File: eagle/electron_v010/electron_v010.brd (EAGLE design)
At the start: 20.3 x 50.8 mm, 92 parts, among them J1 SIM-NANO-4FF, J2 IPEX-20279-001E, U1 U-BLOX-SARA-U260, U2 SN74AVC4T245, U3 STM32F205RG, U4 MAX1704X, U5 SN74LVC1G07, U6 SN74LVC1G07, U8 SN74AVC4T245, X1 USB-MICROB, Y1 32Khz, Y2 26Mhz

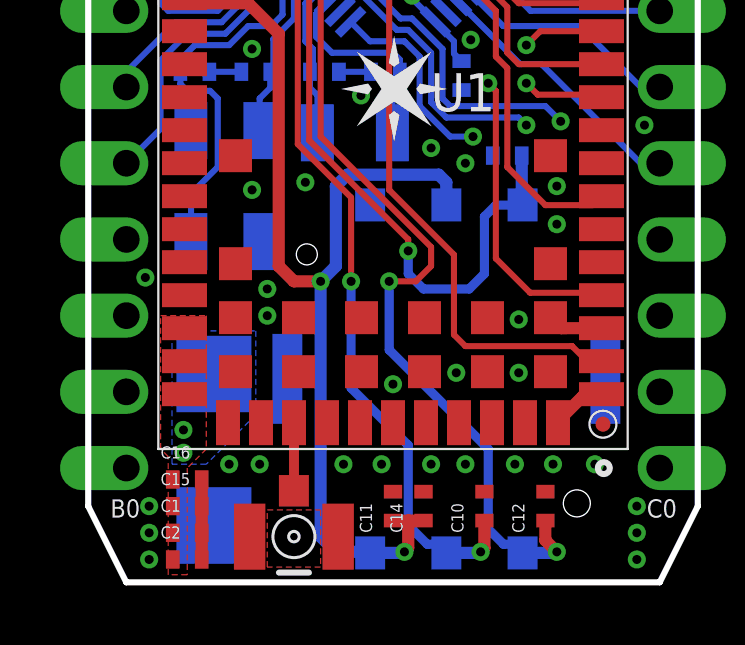
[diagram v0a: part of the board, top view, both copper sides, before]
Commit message: #13 Added more GND Vias around ANT connector and updated trace routes
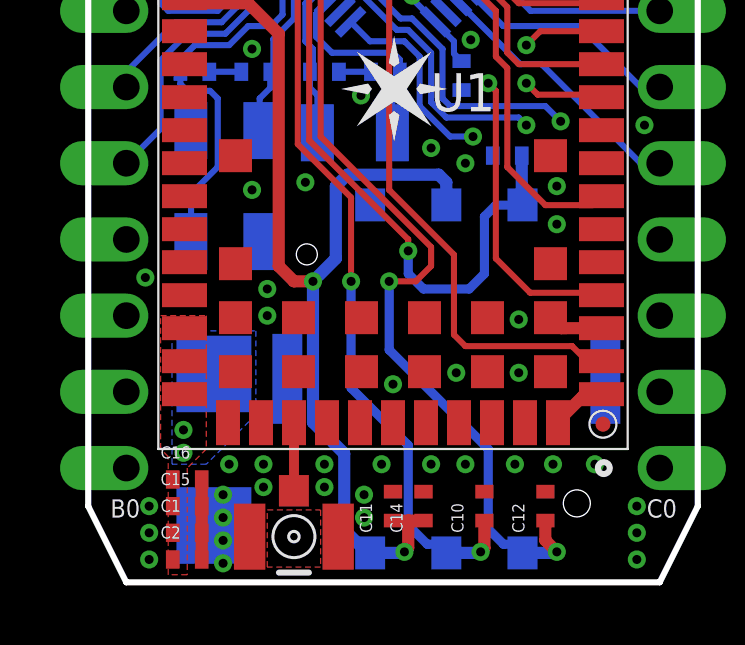
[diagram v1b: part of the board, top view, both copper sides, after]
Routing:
- net SIM_VCC: track 34.7 -> 34.1 mm
- net GND: vias 54 -> 62
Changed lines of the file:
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@@
 <layer number="21" name="tPlace" color="16" fill="1" visible="yes" active="yes"/>
 <layer number="22" name="bPlace" color="14" fill="1" visible="no" active="yes"/>
-<layer number="23" name="tOrigins" color="15" fill="1" visible="yes" active="yes"/>
-<layer number="24" name="bOrigins" color="15" fill="1" visible="yes" active="yes"/>
+<layer number="23" name="tOrigins" color="15" fill="1" visible="no" active="yes"/>
+<layer number="24" name="bOrigins" color="15" fill="1" visible="no" active="yes"/>
 <layer number="25" name="tNames" color="7" fill="1" visible="no" active="yes"/>
 <layer number="26" name="bNames" color="7" fill="1" visible="no" active="yes"/>
@@
 <via x="4.699" y="3.937" extent="1-16" drill="0.3"/>
 <via x="14.224" y="3.937" extent="1-16" drill="0.3"/>
-<via x="8.509" y="3.937" extent="1-16" drill="0.3"/>
+<via x="7.874" y="3.937" extent="1-16" drill="0.3"/>
 <via x="9.779" y="3.937" extent="1-16" drill="0.3"/>
-<via x="5.715" y="3.937" extent="1-16" drill="0.3"/>
+<via x="5.842" y="3.937" extent="1-16" drill="0.3"/>
 <via x="12.573" y="3.937" extent="1-16" drill="0.3"/>
 <via x="11.43" y="3.937" extent="1-16" drill="0.3"/>
@@
 <via x="18.0848" y="43.4594" extent="1-16" drill="0.3"/>
 <contactref element="JP2" pad="15"/>
+<via x="9.1948" y="2.159" extent="1-16" drill="0.3"/>
+<via x="5.842" y="3.175" extent="1-16" drill="0.3"/>
+<via x="7.874" y="3.175" extent="1-16" drill="0.3"/>
+<via x="9.1948" y="2.921" extent="1-16" drill="0.3"/>
+<via x="4.4958" y="2.159" extent="1-16" drill="0.3"/>
+<via x="4.4958" y="2.921" extent="1-16" drill="0.3"/>
+<via x="4.4958" y="1.397" extent="1-16" drill="0.3"/>
+<via x="4.4958" y="0.635" extent="1-16" drill="0.3"/>
 </signal>
 <signal name="N$8">
@@
 <contactref element="C14" pad="1"/>
 <wire x1="10.16" y1="2.0574" x2="10.668" y2="2.0574" width="0.4064" layer="1"/>
-<via x="7.747" y="10.033" extent="1-16" drill="0.3"/>
+<via x="7.493" y="10.033" extent="1-16" drill="0.3"/>
 <wire x1="10.668" y1="2.0574" x2="11.176" y2="2.0574" width="0.4064" layer="1"/>
 <wire x1="3.21" y1="19.472" x2="3.378" y2="19.304" width="0.4064" layer="1"/>
@@
 <wire x1="11.684" y1="13.589" x2="8.636" y2="13.589" width="0.4064" layer="16"/>
 <wire x1="8.636" y1="13.589" x2="8.255" y2="13.208" width="0.4064" layer="16"/>
-<wire x1="8.255" y1="13.208" x2="8.255" y2="10.541" width="0.4064" layer="16"/>
+<wire x1="8.255" y1="13.208" x2="8.255" y2="10.795" width="0.4064" layer="16"/>
 <wire x1="9.3638" y1="1.016" x2="9.398" y2="0.9818" width="0.4064" layer="16"/>
 <via x="10.541" y="1.016" extent="1-16" drill="0.3"/>
@@
 <wire x1="10.541" y1="1.016" x2="10.668" y2="1.143" width="0.4064" layer="1"/>
 <wire x1="10.668" y1="1.143" x2="10.668" y2="2.0574" width="0.4064" layer="1"/>
-<wire x1="8.255" y1="10.541" x2="7.747" y2="10.033" width="0.4064" layer="16"/>
-<wire x1="6.858" y1="10.033" x2="7.747" y2="10.033" width="0.4064" layer="1"/>
-<wire x1="7.747" y1="1.524" x2="7.747" y2="10.033" width="0.4064" layer="16"/>
 <wire x1="5.334" y1="19.304" x2="6.35" y2="18.288" width="0.4064" layer="1"/>
-<wire x1="9.3638" y1="1.016" x2="8.255" y2="1.016" width="0.4064" layer="16"/>
-<wire x1="8.255" y1="1.016" x2="7.747" y2="1.524" width="0.4064" layer="16"/>
+<wire x1="9.3638" y1="1.016" x2="9.271" y2="1.016" width="0.4064" layer="16"/>
+<wire x1="9.271" y1="1.016" x2="8.5344" y2="1.7526" width="0.4064" layer="16"/>
+<wire x1="8.5344" y1="1.7526" x2="8.5344" y2="4.2926" width="0.4064" layer="16"/>
+<wire x1="6.858" y1="10.033" x2="7.493" y2="10.033" width="0.4064" layer="1"/>
+<wire x1="8.255" y1="10.795" x2="7.493" y2="10.033" width="0.4064" layer="16"/>
+<wire x1="7.493" y1="5.334" x2="7.493" y2="10.033" width="0.4064" layer="16"/>
+<wire x1="7.493" y1="5.334" x2="8.5344" y2="4.2926" width="0.4064" layer="16"/>
 </signal>
 <signal name="SIM_RST">

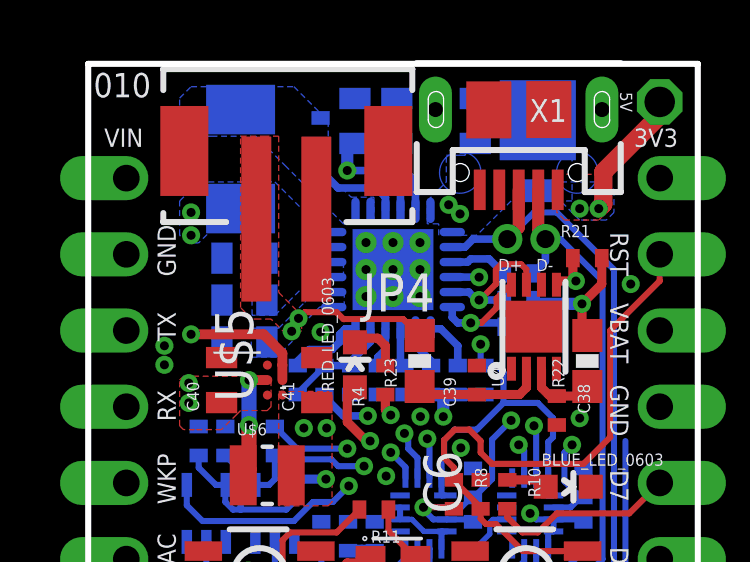
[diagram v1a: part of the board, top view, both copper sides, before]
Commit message: #11 Additional Vias added for battery trace connections
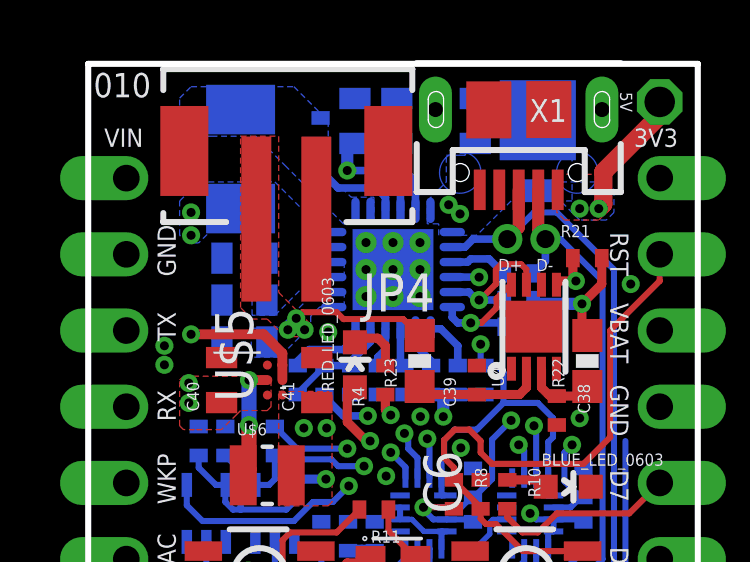
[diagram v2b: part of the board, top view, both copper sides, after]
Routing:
- net BAT: track 4.44 -> 4.52 mm, vias 2 -> 3
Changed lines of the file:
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@@
 </class>
 <class number="3" name="BAT" width="0" drill="0">
-<clearance class="3" value="0.254"/>
+<clearance class="3" value="0.2032"/>
 </class>
 </classes>
@@
 <contactref element="C39" pad="2"/>
 <via x="2.54" y="40.767" extent="1-16" drill="0.3"/>
-<via x="7.747" y="41.8592" extent="1-16" drill="0.3"/>
+<via x="8.001" y="41.8592" extent="1-16" drill="0.3"/>
 <via x="11.0744" y="39.0398" extent="1-16" drill="0.3"/>
 <wire x1="14.351" y1="32.893" x2="13.97" y2="32.893" width="0.2032" layer="16"/>
@@
 <vertex x="7.493" y="45.593"/>
 <vertex x="7.493" y="44.196"/>
-<vertex x="8.509" y="44.196"/>
-<vertex x="8.509" y="43.688"/>
+<vertex x="8.5344" y="44.196"/>
+<vertex x="8.5344" y="43.688"/>
 <vertex x="7.493" y="43.688"/>
 <vertex x="6.223" y="42.418"/>
@@
 <contactref element="JP4" pad="VCC"/>
 <contactref element="R23" pad="2"/>
-<via x="7.0104" y="42.3164" extent="1-16" drill="0.3"/>
+<via x="6.9342" y="42.3164" extent="1-16" drill="0.3"/>
 <wire x1="8.509" y1="42.291" x2="10.502" y2="42.291" width="0.2032" layer="1"/>
 <wire x1="10.502" y1="42.291" x2="11.049" y2="41.744" width="0.2032" layer="1"/>
-<via x="6.7818" y="41.8846" extent="1-16" drill="0.3"/>
+<via x="6.6548" y="41.9354" extent="1-16" drill="0.3"/>
 <wire x1="8.509" y1="42.291" x2="8.2804" y2="42.5196" width="0.2032" layer="1"/>
-<wire x1="8.2804" y1="42.5196" x2="7.2136" y2="42.5196" width="0.2032" layer="1"/>
-<wire x1="7.2136" y1="42.5196" x2="7.0104" y2="42.3164" width="0.2032" layer="1"/>
 <polygon width="0.1524" layer="16" thermals="no" rank="3">
 <vertex x="8.5344" y="43.2054"/>
 <vertex x="8.5344" y="42.6974"/>
-<vertex x="8.4836" y="42.6974"/>
 <vertex x="7.7216" y="42.6974"/>
-<vertex x="7.0358" y="42.0116"/>
-<vertex x="7.0358" y="41.783"/>
-<vertex x="6.2738" y="41.021"/>
+<vertex x="7.4168" y="42.3926"/>
+<vertex x="7.4168" y="41.783"/>
+<vertex x="7.3152" y="41.6814"/>
+<vertex x="7.0358" y="41.6814"/>
+<vertex x="6.3754" y="41.021"/>
 <vertex x="5.4356" y="41.021"/>
-<vertex x="5.4356" y="41.9354"/>
 <vertex x="5.4356" y="41.9862"/>
-<vertex x="5.842" y="41.9862"/>
 <vertex x="6.35" y="41.9862"/>
-<vertex x="7.2136" y="42.8498"/>
 <vertex x="7.5692" y="43.2054"/>
 </polygon>
+<via x="7.2136" y="41.9354" extent="1-16" drill="0.3"/>
+<wire x1="7.1374" y1="42.5196" x2="6.9342" y2="42.3164" width="0.2032" layer="1"/>
 <polygon width="0.1524" layer="1" thermals="no" rank="3">
-<vertex x="6.604" y="41.783"/>
-<vertex x="6.096" y="42.291"/>
-<vertex x="5.715" y="42.291"/>
+<vertex x="5.08" y="48.387"/>
+<vertex x="6.35" y="48.387"/>
+<vertex x="6.35" y="43.18"/>
+<vertex x="7.4168" y="42.1132"/>
+<vertex x="7.4168" y="42.0116"/>
+<vertex x="7.4168" y="41.783"/>
+<vertex x="7.3406" y="41.7068"/>
+<vertex x="6.5532" y="41.7068"/>
+<vertex x="5.969" y="42.291"/>
 <vertex x="5.461" y="42.291"/>
 <vertex x="5.08" y="42.672"/>
-<vertex x="5.08" y="48.387"/>
-<vertex x="5.842" y="48.387"/>
-<vertex x="6.35" y="48.387"/>
-<vertex x="6.35" y="43.18"/>
-<vertex x="6.985" y="42.545"/>
-<vertex x="7.112" y="42.418"/>
-<vertex x="7.112" y="42.164"/>
-<vertex x="7.112" y="41.91"/>
-<vertex x="6.985" y="41.783"/>
 </polygon>
+<wire x1="8.2804" y1="42.5196" x2="7.1374" y2="42.5196" width="0.2032" layer="1"/>
 </signal>
 <signal name="VBUS">
@@
 <contactref element="U$1" pad="12"/>
 <contactref element="R20" pad="2"/>
-<wire x1="8.91" y1="41.967" x2="8.566" y2="41.967" width="0.254" layer="16"/>
-<wire x1="8.566" y1="41.967" x2="8.382" y2="41.783" width="0.254" layer="16"/>
-<wire x1="8.382" y1="41.783" x2="8.382" y2="41.529" width="0.254" layer="16"/>
-<wire x1="8.382" y1="41.529" x2="8.128" y2="41.275" width="0.254" layer="16"/>
-<wire x1="8.128" y1="41.275" x2="7.366" y2="41.275" width="0.254" layer="16"/>
+<wire x1="8.509" y1="41.275" x2="7.366" y2="41.275" width="0.254" layer="16"/>
 <wire x1="7.366" y1="41.275" x2="6.985" y2="40.894" width="0.254" layer="16"/>
 <wire x1="6.985" y1="40.894" x2="6.985" y2="40.7416" width="0.254" layer="16"/>
+<wire x1="8.509" y1="41.275" x2="8.91" y2="41.676" width="0.254" layer="16"/>
+<wire x1="8.91" y1="41.676" x2="8.91" y2="41.967" width="0.254" layer="16"/>
 </signal>
 <signal name="N$7">

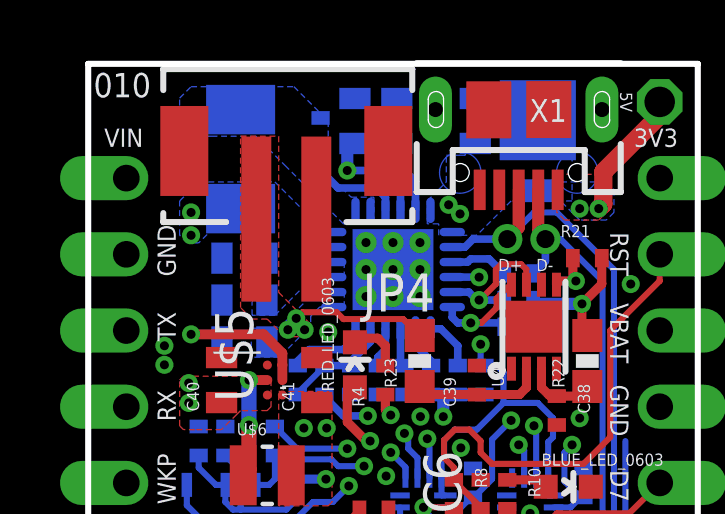
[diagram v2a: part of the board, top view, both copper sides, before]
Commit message: #12 Updated to bigger pads PMIC inductor footprint and power polygons
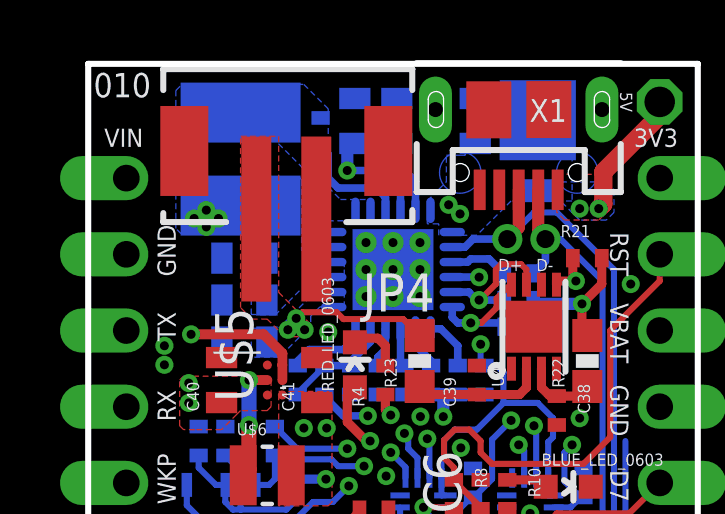
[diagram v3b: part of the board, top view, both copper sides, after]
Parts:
- U$4: device electron:4020TYPE -> Particle:INDUCTOR-4020
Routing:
- net +3V8: track 57.4 -> 56.7 mm, vias 8 -> 10
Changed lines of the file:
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@@
 <element name="JP4" library="SparkFun-Connectors" package="JST-2-SMD-VERT" value="" x="6.604" y="47.625" locked="yes"/>
 <element name="U$3" library="Spark" package="DIODE-DO-220AA(SMP)" value="DIODE" x="14.986" y="48.9204" locked="yes" rot="MR270"/>
-<element name="U$4" library="electron" package="4020TYPE" value="2.2uH" x="5.08" y="47.625" locked="yes" rot="MR270"/>
+<element name="U$4" library="Particle" package="INDUCTOR-4020" value="2.2uH" x="5.08" y="47.625" locked="yes" rot="MR270"/>
 <element name="RED_LED_0603" library="SparkFun" package="LED-0603" value="" x="8.89" y="40.767" locked="yes"/>
 <element name="R2" library="Spark" package="R0402_B" value="333R" x="9.652" y="40.259" locked="yes" rot="MR270"/>
@@
 <via x="3.3528" y="39.497" extent="1-16" drill="0.3"/>
 <via x="9.398" y="38.227" extent="1-16" drill="0.3"/>
-<via x="3.429" y="45.847" extent="1-16" drill="0.3"/>
-<via x="3.429" y="45.085" extent="1-16" drill="0.3"/>
+<via x="3.937" y="45.9232" extent="1-16" drill="0.3"/>
+<via x="3.937" y="45.3644" extent="1-16" drill="0.3"/>
 <via x="3.175" y="5.08" extent="1-16" drill="0.3"/>
 <wire x1="3.937" y1="5.842" x2="3.175" y2="5.08" width="1.778" layer="2"/>
 <wire x1="3.175" y1="5.08" x2="3.175" y2="4.318" width="1.778" layer="2"/>
-<wire x1="3.429" y1="45.085" x2="3.429" y2="45.847" width="1.778" layer="2"/>
 <polygon width="0.1524" layer="16" thermals="no">
 <vertex x="2.794" y="8.382"/>
@@
 <vertex x="3.937" y="3.937"/>
 <vertex x="2.794" y="3.937"/>
-</polygon>
-<polygon width="0.1524" layer="16" thermals="no">
-<vertex x="3.048" y="46.228"/>
-<vertex x="3.683" y="46.863"/>
-<vertex x="6.223" y="46.863"/>
-<vertex x="7.493" y="45.593"/>
-<vertex x="7.493" y="44.196"/>
-<vertex x="8.5344" y="44.196"/>
-<vertex x="8.5344" y="43.688"/>
-<vertex x="7.493" y="43.688"/>
-<vertex x="6.223" y="42.418"/>
-<vertex x="5.461" y="42.418"/>
-<vertex x="5.461" y="45.339"/>
-<vertex x="4.191" y="45.339"/>
-<vertex x="3.683" y="44.831"/>
-<vertex x="3.302" y="44.831"/>
-<vertex x="3.048" y="45.085"/>
 </polygon>
 <wire x1="9.271" y1="38.227" x2="8.636" y2="38.862" width="0.3048" layer="15"/>
@@
 <wire x1="3.937" y1="31.877" x2="3.937" y2="39.497" width="1.778" layer="2"/>
 <wire x1="3.937" y1="39.497" x2="3.937" y2="41.783" width="1.778" layer="2"/>
-<wire x1="3.937" y1="41.783" x2="3.937" y2="44.577" width="1.778" layer="2"/>
-<wire x1="3.429" y1="45.085" x2="3.937" y2="44.577" width="1.778" layer="2"/>
+<wire x1="3.937" y1="41.783" x2="3.937" y2="45.3644" width="1.778" layer="2"/>
 <polygon width="0.1524" layer="1" thermals="no">
 <vertex x="2.413" y="8.89"/>
@@
 <wire x1="5.842" y1="41.783" x2="3.429" y2="41.783" width="0.3302" layer="1"/>
 <wire x1="3.429" y1="41.783" x2="3.937" y2="41.783" width="0.508" layer="2"/>
+<via x="3.5306" y="45.6438" extent="1-16" drill="0.3"/>
+<via x="4.3434" y="45.6438" extent="1-16" drill="0.3"/>
+<polygon width="0.1524" layer="16" thermals="no">
+<vertex x="8.5344" y="43.942"/>
+<vertex x="8.5344" y="43.688"/>
+<vertex x="8.255" y="43.688"/>
+<vertex x="7.493" y="43.688"/>
+<vertex x="6.2484" y="42.4434"/>
+<vertex x="5.4356" y="42.4434"/>
+<vertex x="5.4356" y="43.815"/>
+<vertex x="5.4356" y="44.831"/>
+<vertex x="5.1308" y="45.1358"/>
+<vertex x="3.0988" y="45.1358"/>
+<vertex x="2.921" y="45.3136"/>
+<vertex x="2.921" y="46.8122"/>
+<vertex x="3.1242" y="47.0154"/>
+<vertex x="7.0358" y="47.0154"/>
+<vertex x="7.112" y="46.9392"/>
+<vertex x="7.112" y="44.6024"/>
+<vertex x="7.493" y="44.2214"/>
+<vertex x="8.5344" y="44.2214"/>
+</polygon>
 </signal>
 <signal name="SIM_VCC">
@@
 <contactref element="U$4" pad="P$1"/>
 <contactref element="C7" pad="2"/>
-<polygon width="0.1524" layer="16" thermals="no">
-<vertex x="9.525" y="45.466"/>
-<vertex x="8.509" y="45.466"/>
-<vertex x="6.604" y="47.371"/>
-<vertex x="5.588" y="48.387"/>
-<vertex x="4.191" y="48.387"/>
-<vertex x="3.429" y="48.387"/>
-<vertex x="3.048" y="48.768"/>
-<vertex x="3.048" y="49.657"/>
-<vertex x="3.429" y="50.038"/>
-<vertex x="6.858" y="50.038"/>
-<vertex x="8.001" y="48.895"/>
-<vertex x="8.001" y="47.117"/>
-<vertex x="8.763" y="46.355"/>
-<vertex x="9.525" y="46.355"/>
+<polygon width="0.1524" layer="16" thermals="no" rank="2">
+<vertex x="9.144" y="45.5676"/>
+<vertex x="7.5692" y="45.5676"/>
+<vertex x="7.4422" y="45.6946"/>
+<vertex x="7.4422" y="47.0408"/>
+<vertex x="7.1628" y="47.3202"/>
+<vertex x="6.2484" y="48.2346"/>
+<vertex x="4.572" y="48.2346"/>
+<vertex x="3.1242" y="48.2346"/>
+<vertex x="2.921" y="48.4378"/>
+<vertex x="2.921" y="49.911"/>
+<vertex x="3.1242" y="50.1142"/>
+<vertex x="7.1882" y="50.1142"/>
+<vertex x="8.001" y="49.3014"/>
+<vertex x="8.001" y="46.6852"/>
+<vertex x="8.4074" y="46.2788"/>
+<vertex x="9.4234" y="46.2788"/>
+<vertex x="9.4234" y="45.5676"/>
 </polygon>
 </signal>
@@
 <wire x1="9.91" y1="46.351" x2="9.6012" y2="46.6598" width="0.254" layer="16"/>
 <wire x1="9.6012" y1="46.6598" x2="8.3312" y2="46.6598" width="0.254" layer="16"/>
-<wire x1="8.3312" y1="46.6598" x2="7.747" y2="47.244" width="0.254" layer="16"/>
-<wire x1="7.747" y1="47.244" x2="7.747" y2="48.0314" width="0.254" layer="16"/>
+<wire x1="8.3312" y1="46.6598" x2="8" y2="46.991" width="0.254" layer="16"/>
+<wire x1="8" y1="46.991" x2="8" y2="47.7784" width="0.254" layer="16"/>
+<wire x1="8" y1="47.7784" x2="7.747" y2="48.0314" width="0.254" layer="16"/>
 </signal>
 <signal name="BAT" class="3">

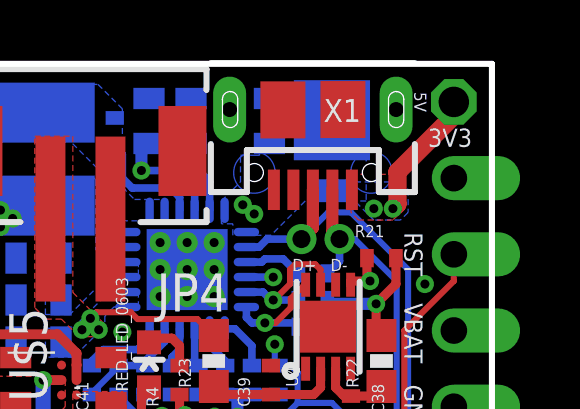
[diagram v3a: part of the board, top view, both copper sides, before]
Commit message: Updated 5V header pad to round with drill size same as other headers
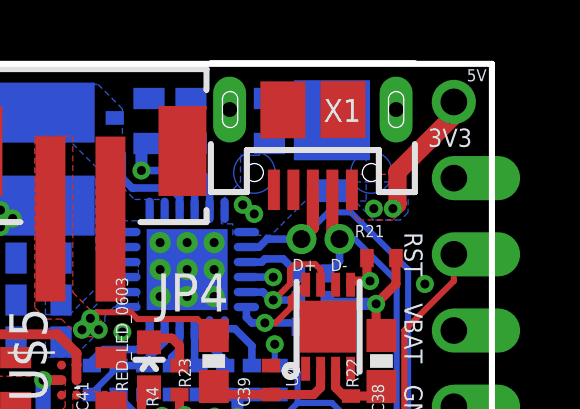
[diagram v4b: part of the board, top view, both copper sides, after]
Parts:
- JP3: device pinhead:1X01 -> Particle:1X01
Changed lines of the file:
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@@
 <wire x1="104.14" y1="35.56" x2="26.67" y2="35.56" width="0.127" layer="51"/>
 <wire x1="26.67" y1="35.56" x2="26.67" y2="10.16" width="0.127" layer="51"/>
-<text x="18.1356" y="49.8602" size="0.4064" layer="21" font="vector" ratio="12" rot="SR270" align="top-left">5V</text>
+<text x="19.4818" y="50.6222" size="0.4064" layer="21" font="vector" ratio="12" rot="SR0" align="top-left">5V</text>
 <text x="18.1864" y="48.641" size="0.6096" layer="21" font="vector" ratio="12" rot="SR0" align="top-left">3V3</text>
 <text x="18.0086" y="45.1866" size="0.6096" layer="21" font="vector" ratio="12" rot="SR270" align="top-left">RST</text>
@@
 <element name="U$7" library="Particle" package="M02_0.05_HEADER" value="M02_0.05_HEADER" x="14.605" y="44.958" locked="yes"/>
 <element name="C39" library="Spark" package="C0402_B" value="1uF" x="12.954" y="40.259" locked="yes" rot="R90"/>
-<element name="JP3" library="pinhead" package="1X01" value="" x="19.05" y="49.53" locked="yes" rot="MR0"/>
+<element name="JP3" library="Particle" package="1X01" value="" x="19.05" y="49.53" locked="yes" rot="MR0"/>
 <element name="JP2" library="Particle" package="1X18-D-PADS" value="M18DPAD" x="19.05" y="25.4" locked="yes" rot="MR90"/>
 </elements>
